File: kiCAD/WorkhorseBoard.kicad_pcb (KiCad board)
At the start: 2 copper layers, 392 parts, among them J1 USB_B_Mini, J10 MAIN_POWER, J11 BED_POWER, J12 H0, J13 F0, J14 V_SELECT, J15 F1, J16 F4, J17 H1, J18 V_SELECT, J19 F2, J2 Micro_SD_Card, J20 F5, J21 H2, J22 F3, J23 HB, J24 Conn_01x02, J25 Conn_01x02, J26 Conn_01x02, J27 Conn_01x02, J28 Conn_01x03, J29 Conn_01x03, J3 Conn_01x06, J30 Conn_01x03, J31 Conn_01x03, J32 Conn_01x03, J33 Conn_01x03, J4 X, J5 E0, J6 Y, J7 E1, J8 Z, J9 E2, Q1 Q_NMOS_GSD, Q10 Q_NMOS_GDS, Q2 Q_NMOS_GDS, Q3 Q_NMOS_GSD, Q4 Q_NMOS_GSD, Q5 Q_NMOS_GDS, Q6 Q_NMOS_GSD, Q7 Q_NMOS_GSD, Q8 Q_NMOS_GDS, Q9 Q_NMOS_GSD, SW1 SW_Push, U1 24C02, U10 TPS54531, U11 TPS54531, U12 AP7361C-33E-13, U13 74HCT365, U14 74HCT365, U2 USBLC6-2SC6, U3 STM32F446VETx, U4 TMC2209, U5 TMC2209, U6 TMC2209, U7 TMC2209, U8 TMC2209, U9 TMC2209, Y1 X322512MSB4SI

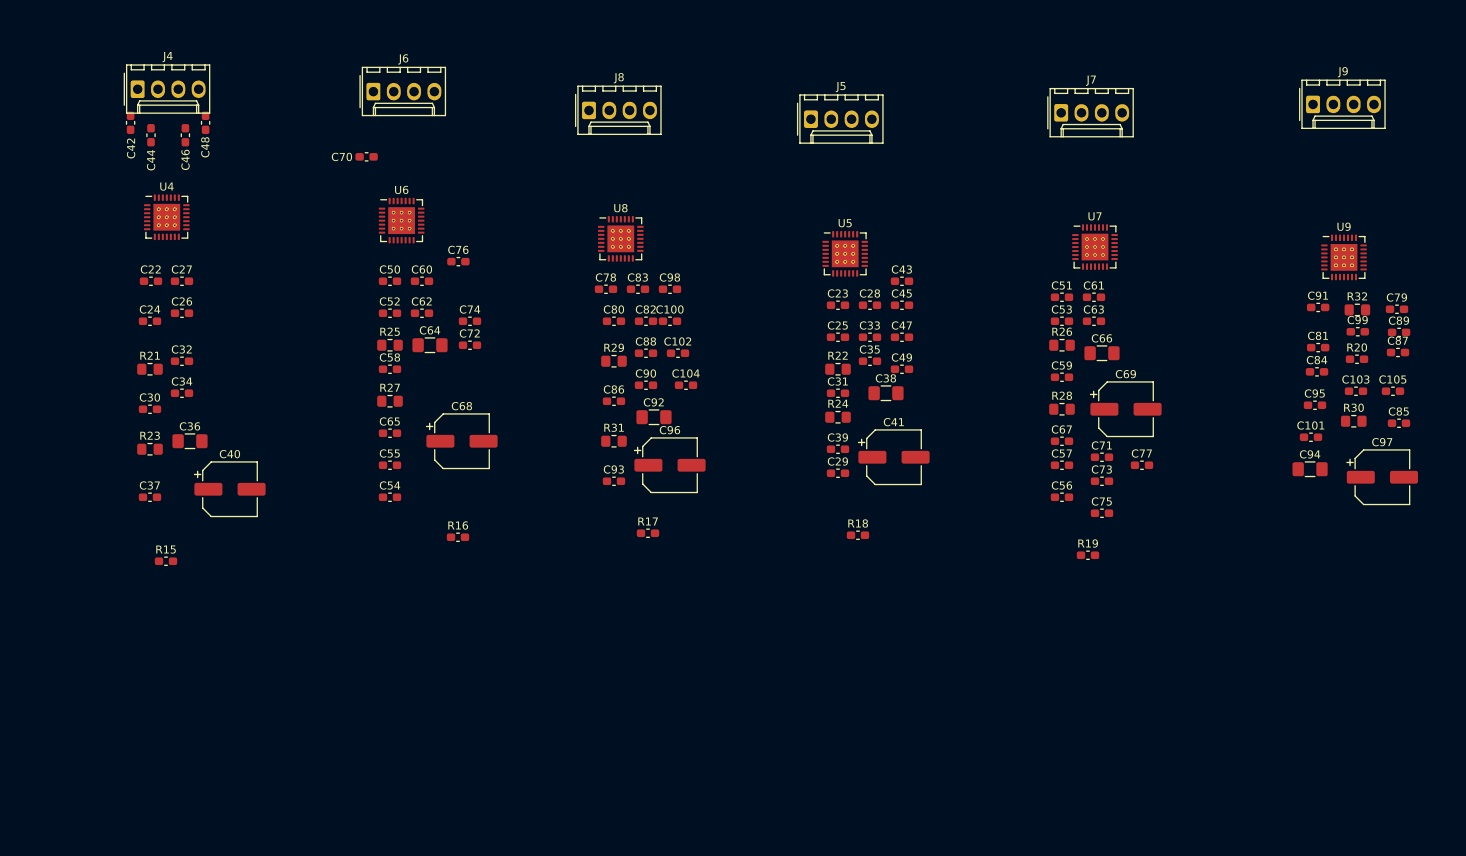
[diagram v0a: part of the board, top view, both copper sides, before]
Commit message: started laying out drivers
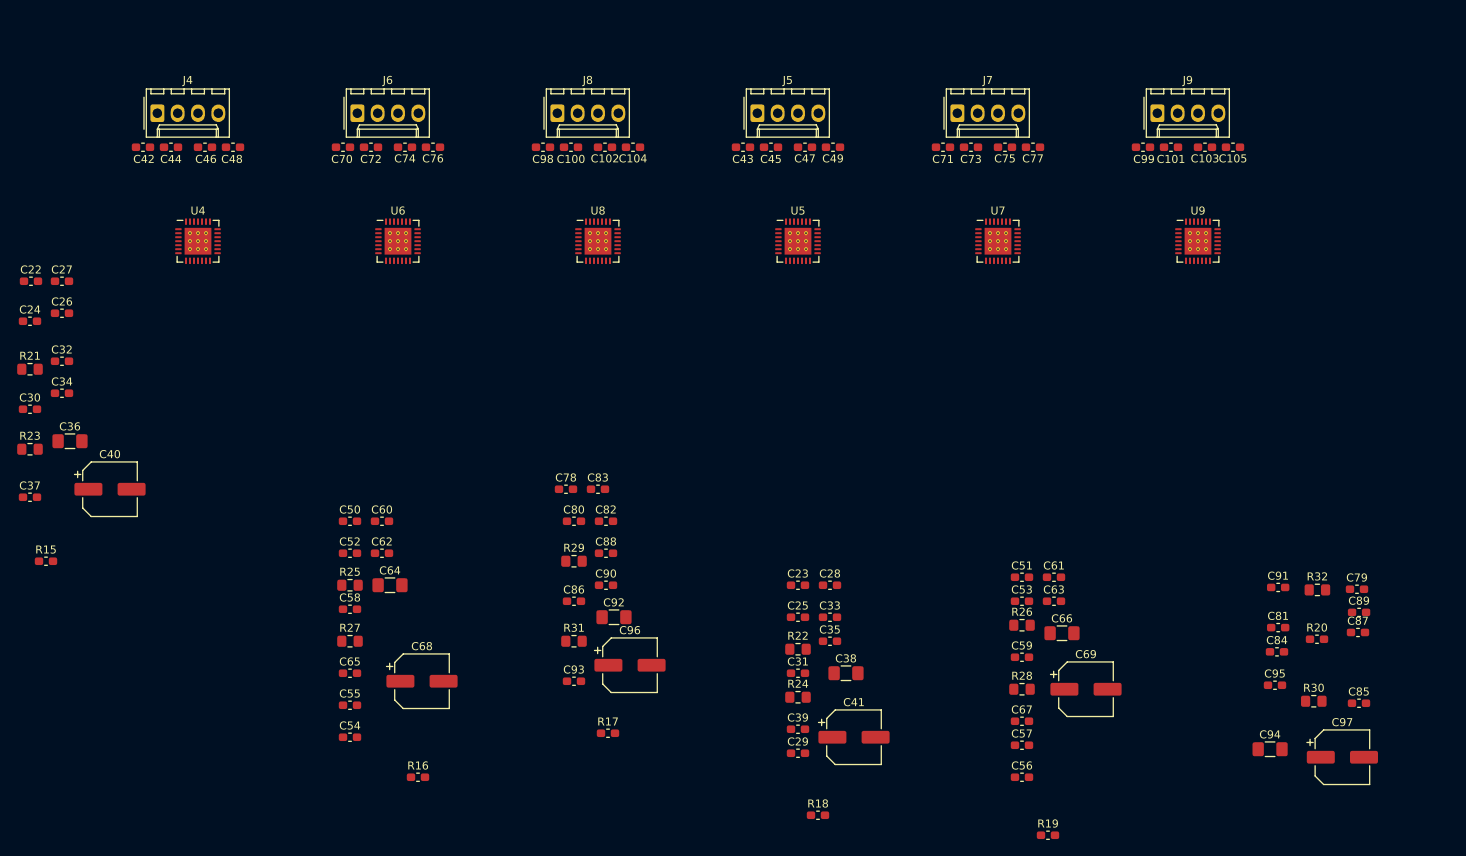
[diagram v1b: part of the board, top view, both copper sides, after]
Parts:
- moved C75 47.3 mm to (140.9, 38.2), turned to 180 degrees
- moved C73 44.8 mm to (136.6, 38.2)
- moved C71 43.5 mm to (133.1, 38.2)
- moved C77 42.0 mm to (144.4, 38.2), turned to 180 degrees
- moved C101 40.3 mm to (161.6, 38.2)
- moved C105 36.5 mm to (169.4, 38.2), turned to 180 degrees
- moved C103 35.9 mm to (165.9, 38.2), turned to 180 degrees
- moved C99 35.4 mm to (158.1, 38.2)
- moved C91 35.4 mm to (175.0, 93.3)
- moved C23 35.4 mm to (115.0, 93.0)
- moved C25 35.4 mm to (115.0, 97.0)
- moved C28 35.4 mm to (119.0, 93.0)
- moved C29 35.4 mm to (115.0, 114.0)
- moved C31 35.4 mm to (115.0, 104.0)
- moved C33 35.4 mm to (119.0, 97.0)
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
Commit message: layed out TMC's and started laying out power electronics
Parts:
- moved Q10 292.9 mm to (50.5, 177.2), turned to 180 degrees
- moved J23 277.1 mm to (36.5, 167.2), turned to 270 degrees
- moved H3 261.3 mm to (36.0, 189.2)
- moved C139 255.1 mm to (245.0, 134.8)
- moved D14 255.1 mm to (223.6, 125.4)
- moved D16 255.1 mm to (246.4, 146.3)
- moved D24 255.1 mm to (259.4, 132.5)
- moved D25 255.1 mm to (243.1, 138.5)
- moved J16 255.1 mm to (220.4, 149.3)
- moved J17 255.1 mm to (187.2, 146.3)
- moved JP6 255.1 mm to (242.7, 108.9)
- moved Q3 255.1 mm to (254.1, 121.2)
- moved Q6 255.1 mm to (262.6, 113.4)
- moved Q9 255.1 mm to (255.4, 116.7)
- moved R44 255.1 mm to (247.4, 137.7)
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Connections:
- C100 pad 2: Net-(C100-Pad2) -> Z_OB1
- C101 pad 2: Net-(C101-Pad2) -> E2_OB1
- C102 pad 2: Net-(C102-Pad2) -> Z_OA1
- C103 pad 2: Net-(C103-Pad2) -> E2_OA1
- C104 pad 2: Net-(C104-Pad2) -> Z_OA2
- C105 pad 2: Net-(C105-Pad2) -> E2_OA2
- C42 pad 2: Net-(C42-Pad2) -> X_OB2
- C43 pad 2: Net-(C43-Pad2) -> E0_OB2
- C44 pad 2: Net-(C44-Pad2) -> X_OB1
- C45 pad 2: Net-(C45-Pad2) -> E0_OB1
- C46 pad 2: Net-(C46-Pad2) -> X_OA1
- C47 pad 2: Net-(C47-Pad2) -> E0_OA1
- C48 pad 2: Net-(C48-Pad2) -> X_OA2
- C49 pad 2: Net-(C49-Pad2) -> E0_OA2
- C70 pad 2: Net-(C70-Pad2) -> Y_OB2
- C71 pad 2: Net-(C71-Pad2) -> E1_OB2
- C72 pad 2: Net-(C72-Pad2) -> Y_OB1
- C73 pad 2: Net-(C73-Pad2) -> E1_OB1
- C74 pad 2: Net-(C74-Pad2) -> Y_OA1
- C75 pad 2: Net-(C75-Pad2) -> E1_OA1
- C76 pad 2: Net-(C76-Pad2) -> Y_OA2
- C77 pad 2: Net-(C77-Pad2) -> E1_OA2
- C98 pad 2: Net-(C98-Pad2) -> Z_OB2
- C99 pad 2: Net-(C99-Pad2) -> E2_OB2
- J4 pad 1: Net-(C42-Pad2) -> X_OB2
- J4 pad 2: Net-(C44-Pad2) -> X_OB1
- J4 pad 3: Net-(C46-Pad2) -> X_OA1
- J4 pad 4: Net-(C48-Pad2) -> X_OA2
- J5 pad 1: Net-(C43-Pad2) -> E0_OB2
- J5 pad 2: Net-(C45-Pad2) -> E0_OB1
- J5 pad 3: Net-(C47-Pad2) -> E0_OA1
- J5 pad 4: Net-(C49-Pad2) -> E0_OA2
- J6 pad 1: Net-(C70-Pad2) -> Y_OB2
- J6 pad 2: Net-(C72-Pad2) -> Y_OB1
- J6 pad 3: Net-(C74-Pad2) -> Y_OA1
- J6 pad 4: Net-(C76-Pad2) -> Y_OA2
- J7 pad 1: Net-(C71-Pad2) -> E1_OB2
- J7 pad 2: Net-(C73-Pad2) -> E1_OB1
- J7 pad 3: Net-(C75-Pad2) -> E1_OA1
- J7 pad 4: Net-(C77-Pad2) -> E1_OA2
- J8 pad 1: Net-(C98-Pad2) -> Z_OB2
- J8 pad 2: Net-(C100-Pad2) -> Z_OB1
- J8 pad 3: Net-(C102-Pad2) -> Z_OA1
- J8 pad 4: Net-(C104-Pad2) -> Z_OA2
- J9 pad 1: Net-(C99-Pad2) -> E2_OB2
- J9 pad 2: Net-(C101-Pad2) -> E2_OB1
- J9 pad 3: Net-(C103-Pad2) -> E2_OA1
- J9 pad 4: Net-(C105-Pad2) -> E2_OA2
- U4 pad 1: Net-(C48-Pad2) -> X_OB2
- U4 pad 21: Net-(C44-Pad2) -> X_OA2
- U4 pad 24: Net-(C42-Pad2) -> X_OA1
- U4 pad 26: Net-(C46-Pad2) -> X_OB1
- U5 pad 1: Net-(C49-Pad2) -> E0_OB2
- U5 pad 21: Net-(C45-Pad2) -> E0_OA2
- U5 pad 24: Net-(C43-Pad2) -> E0_OA1
- U5 pad 26: Net-(C47-Pad2) -> E0_OB1
- U6 pad 1: Net-(C76-Pad2) -> Y_OB2
- U6 pad 21: Net-(C72-Pad2) -> Y_OA2
- U6 pad 24: Net-(C70-Pad2) -> Y_OA1
- U6 pad 26: Net-(C74-Pad2) -> Y_OB1
- U7 pad 1: Net-(C77-Pad2) -> E1_OB2
- U7 pad 21: Net-(C73-Pad2) -> E1_OA2
- U7 pad 24: Net-(C71-Pad2) -> E1_OA1
- U7 pad 26: Net-(C75-Pad2) -> E1_OB1
- U8 pad 1: Net-(C104-Pad2) -> Z_OB2
- U8 pad 21: Net-(C100-Pad2) -> Z_OA2
- U8 pad 24: Net-(C98-Pad2) -> Z_OA1
- U8 pad 26: Net-(C102-Pad2) -> Z_OB1
- U9 pad 1: Net-(C105-Pad2) -> E2_OB2
- U9 pad 21: Net-(C101-Pad2) -> E2_OA2
- U9 pad 24: Net-(C99-Pad2) -> E2_OA1
- U9 pad 26: Net-(C103-Pad2) -> E2_OB1

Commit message: fixed placement slightly to improve cooling
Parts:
- moved C107 323.1 mm to (318.9, -26.2)
- moved C109 323.1 mm to (318.9, -24.6)
- moved C111 323.1 mm to (318.2, -29.5)
- moved D2 323.1 mm to (315.2, -29.1)
- moved F3 323.1 mm to (307.9, -24.9)
- moved J11 323.1 mm to (297.5, -46.4)
- moved J23 323.1 mm to (297.5, -23.1)
- moved Q10 323.1 mm to (311.5, -13.2)
- moved D4 313.3 mm to (320.2, -32.7), turned to 270 degrees
- moved R34 308.0 mm to (320.3, -28.9), turned to 90 degrees
- moved D9 63.8 mm to (66.0, 104.4), turned to 180 degrees
- moved D8 56.6 mm to (66.0, 122.9), turned to 180 degrees
- moved C124 34.0 mm to (67.5, 127.2), turned to 180 degrees
- moved C89 27.5 mm to (198.6, 41.2), turned to 180 degrees
- moved C79 27.1 mm to (218.6, 55.5)
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
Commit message: did layout for FETs and redid layout for Power input
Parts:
- removed J14, J18: V_SELECT, Connector_PinHeader_2.54mm:PinHeader_2x03_P2.54mm_Vertical
- added JP19: Jumper_3_Open, Connector_PinHeader_2.54mm:PinHeader_1x03_P2.54mm_Vertical, F.Cu at (153.8, 104.0)
- added JP20: Jumper_3_Open, Connector_PinHeader_2.54mm:PinHeader_1x03_P2.54mm_Vertical, F.Cu at (163.0, 104.0)
- moved D4 294.2 mm to (48.2, 79.5)
- moved R34 294.1 mm to (48.2, 82.9)
- moved Q10 291.9 mm to (49.6, 115.8)
- moved D2 291.1 mm to (45.8, 81.0)
- moved F3 289.8 mm to (45.9, 98.8)
- moved J11 288.7 mm to (35.5, 74.8)
- moved J23 288.7 mm to (35.5, 98.1)
- moved C107 288.6 mm to (51.9, 83.3)
- moved C109 288.6 mm to (51.9, 84.9)
- moved C111 288.3 mm to (51.5, 80.0)
- moved D36 208.3 mm to (48.6, 120.2)
- moved C147 204.4 mm to (48.5, 105.0), turned to 90 degrees
- moved R67 201.8 mm to (50.8, 104.6), turned to 270 degrees
- moved R47 197.7 mm to (250.4, 71.8)
- moved R53 197.7 mm to (246.1, 71.8)
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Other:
- copper layers 2 -> 4

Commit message: finished layout of everything but endstops.
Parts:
- removed C18: 100n, Capacitor_SMD:C_0603_1608Metric_Pad1.05x0.95mm_HandSolder
- removed C19: 1u, Capacitor_SMD:C_0603_1608Metric_Pad1.05x0.95mm_HandSolder
- removed D13, D18, D25: LED_Small, Diode_SMD:D_0603_1608Metric_Pad1.05x0.95mm_HandSolder
- removed R56, R60, R64: 2.2k, Resistor_SMD:R_0603_1608Metric_Pad1.05x0.95mm_HandSolder
- moved JP13 195.0 mm to (334.7, 92.2), turned to 90 degrees
- moved JP17 183.3 mm to (318.2, 92.8), turned to 90 degrees
- moved R18 180.3 mm to (126.2, 93.1), turned to 90 degrees
- moved SWD1 179.7 mm to (208.8, 113.8), turned to 90 degrees
- moved UART1 178.7 mm to (217.3, 122.5), turned to 270 degrees
- moved JP10 178.5 mm to (335.0, 75.2), turned to 90 degrees
- moved JP18 177.4 mm to (318.5, 75.8), turned to 90 degrees
- moved C152 177.1 mm to (374.9, 74.2)
- moved C153 177.1 mm to (370.6, 78.8)
- moved C154 177.1 mm to (365.9, 83.5)
- moved C155 177.1 mm to (379.9, 70.9)
- moved C156 177.1 mm to (370.3, 81.3)
- moved C157 177.1 mm to (374.9, 76.7)
- moved D41 177.1 mm to (375.6, 66.6)
- moved D42 177.1 mm to (361.6, 81.0)
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
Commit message: Started tracing
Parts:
- moved C155 196.9 mm to (183.8, 89.1), turned to 90 degrees
- moved JP12 195.8 mm to (186.5, 87.5)
- moved R88 192.9 mm to (187.5, 81.9), turned to 270 degrees
- moved R80 192.8 mm to (187.4, 70.1), turned to 270 degrees
- moved C152 191.5 mm to (183.7, 65.6), turned to 90 degrees
- moved R87 188.6 mm to (191.8, 93.6), turned to 90 degrees
- moved C156 186.6 mm to (183.8, 77.4), turned to 90 degrees
- moved D41 185.4 mm to (190.2, 70.1), turned to 270 degrees
- moved JP7 180.0 mm to (186.4, 64.0)
- moved R85 178.9 mm to (187.5, 93.6), turned to 270 degrees
- moved R90 178.3 mm to (192.0, 81.9), turned to 90 degrees
- moved C157 172.2 mm to (203.2, 89.4), turned to 90 degrees
- moved JP15 170.6 mm to (186.5, 75.7)
- moved R82 170.2 mm to (191.7, 70.1), turned to 90 degrees
- moved R89 170.0 mm to (207.0, 93.9), turned to 270 degrees
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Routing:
- net GND: track 0.00 -> 358.9 mm, vias 0 -> 3
- net +24V: track 0.00 -> 173.6 mm
- net +3V3: track 0.00 -> 138.5 mm
- net +5V: track 0.00 -> 134.1 mm
- net VM: track 0.00 -> 96.4 mm
- net Net-(Q10-Pad1): track 0.00 -> 90.5 mm, vias 0 -> 2
- net +12V: track 0.00 -> 87.0 mm
- net VBED: track 0.00 -> 46.1 mm
- net Net-(Q2-Pad1): track 0.00 -> 31.2 mm, vias 0 -> 2
- net Net-(C147-Pad1): track 0.00 -> 30.6 mm
- net Net-(C138-Pad1): track 0.00 -> 27.0 mm
- net Net-(C144-Pad1): track 0.00 -> 25.5 mm
- net Net-(C142-Pad1): track 0.00 -> 24.7 mm
- net Net-(C129-Pad1): track 0.00 -> 21.7 mm
- net Net-(C128-Pad1): track 0.00 -> 20.5 mm
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- added copper zone on F.Cu, net +12V
- added copper zone on F.Cu, net +24V
- added copper zone on F.Cu, net +3V3
- added copper zone on F.Cu, net +5V
- added copper zone on B.Cu, net GND
- added copper zone on F.Cu, net GND
- added copper zone on In1.Cu, net GND
- added copper zone on F.Cu, net VM
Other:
- board outline added: 205 x 97 mm

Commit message: small changes.
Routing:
- net +24V: track 173.6 -> 248.9 mm
- net VM: track 96.4 -> 98.4 mm
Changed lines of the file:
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@@
     (thickness 1.6)
     (drawings 9)
-    (tracks 1137)
+    (tracks 1172)
     (zones 0)
     (modules 384)
@@
   (segment (start 166.5 41.25) (end 166.5 38.25) (width 0.5) (layer F.Cu) (net 15))
   (segment (start 196.5 41.25) (end 196.5 38.25) (width 0.5) (layer F.Cu) (net 15))
+  (segment (start 184.75 48) (end 184.75 46) (width 0.5) (layer F.Cu) (net 15))
   (segment (start 54.05 54) (end 49.812986 54) (width 0.3) (layer F.Cu) (net 16))
   (segment (start 48.312986 52.5) (end 48 52.5) (width 0.3) (layer F.Cu) (net 16))
@@
   (segment (start 59.5 68.5) (end 61.25 70.25) (width 0.7) (layer F.Cu) (net 49))
   (segment (start 59.5 66.75) (end 59.5 68.5) (width 0.7) (layer F.Cu) (net 49))
-  (segment (start 78.5 108.5) (end 78.5 106.25) (width 1) (layer F.Cu) (net 49))
   (segment (start 81.5 109.5) (end 79.5 109.5) (width 1) (layer F.Cu) (net 49))
   (segment (start 79.5 109.5) (end 78.5 108.5) (width 1) (layer F.Cu) (net 49))
@@
   (segment (start 41.5 76.25) (end 50.25 76.25) (width 0.5) (layer F.Cu) (net 49))
   (segment (start 50.25 76.25) (end 53.75 79.75) (width 0.5) (layer F.Cu) (net 49))
+  (segment (start 79.5 113.14) (end 80.5 114.14) (width 2) (layer F.Cu) (net 49))
+  (segment (start 79.5 109.5) (end 79.5 109.75) (width 2) (layer F.Cu) (net 49))
+  (segment (start 79.5 109.75) (end 80.25 110.5) (width 2) (layer F.Cu) (net 49))
+  (segment (start 80.25 111) (end 79.5 111.75) (width 2) (layer F.Cu) (net 49))
+  (segment (start 80.25 110.5) (end 80.25 111) (width 2) (layer F.Cu) (net 49))
+  (segment (start 79.5 111.75) (end 79.5 113.14) (width 2) (layer F.Cu) (net 49))
+  (segment (start 80.75 109.5) (end 78.5 107.25) (width 2) (layer F.Cu) (net 49))
+  (segment (start 78.5 108.5) (end 78.5 107.25) (width 1) (layer F.Cu) (net 49))
+  (segment (start 81.5 109.5) (end 80.75 109.5) (width 2) (layer F.Cu) (net 49))
+  (segment (start 78.5 107.25) (end 78.5 106.25) (width 1) (layer F.Cu) (net 49))
+  (segment (start 99.5 109.25) (end 96.5 106.25) (width 2) (layer F.Cu) (net 49))
+  (segment (start 63.5 109.25) (end 60.5 106.25) (width 2) (layer F.Cu) (net 49))
+  (segment (start 63.5 109.5) (end 63.5 109.25) (width 2) (layer F.Cu) (net 49))
+  (segment (start 81.5 109.25) (end 78.5 106.25) (width 2) (layer F.Cu) (net 49))
+  (segment (start 81.5 109.5) (end 81.5 109.25) (width 2) (layer F.Cu) (net 49))
+  (segment (start 98.5 113.89) (end 95.64 113.89) (width 2) (layer F.Cu) (net 49))
+  (segment (start 95.64 113.89) (end 94.75 113) (width 2) (layer F.Cu) (net 49))
+  (segment (start 94.75 113) (end 94.75 106.25) (width 2) (layer F.Cu) (net 49))
+  (segment (start 94.75 106.25) (end 96.5 106.25) (width 2) (layer F.Cu) (net 49))
+  (segment (start 76.5 106.25) (end 78.5 106.25) (width 2) (layer F.Cu) (net 49))
+  (segment (start 76.5 108.25) (end 77.25 108.25) (width 2) (layer F.Cu) (net 49))
+  (segment (start 76.5 108.25) (end 76.5 106.25) (width 2) (layer F.Cu) (net 49))
+  (segment (start 77.25 108.25) (end 78.75 109.75) (width 2) (layer F.Cu) (net 49))
+  (segment (start 78.75 109.75) (end 78.75 110.75) (width 2) (layer F.Cu) (net 49))
+  (segment (start 78.75 110.75) (end 78.25 111.25) (width 2) (layer F.Cu) (net 49))
+  (segment (start 77.64 114.14) (end 76.5 113) (width 2) (layer F.Cu) (net 49))
+  (segment (start 80.5 114.14) (end 77.64 114.14) (width 2) (layer F.Cu) (net 49))
+  (segment (start 76.5 113) (end 76.5 108.25) (width 2) (layer F.Cu) (net 49))
+  (segment (start 80.5 114.14) (end 79.89 114.14) (width 2) (layer F.Cu) (net 49))
+  (segment (start 78.5 112.75) (end 78.5 106.25) (width 2) (layer F.Cu) (net 49))
+  (segment (start 79.89 114.14) (end 78.5 112.75) (width 2) (layer F.Cu) (net 49))
+  (segment (start 62.5 114.14) (end 60.14 114.14) (width 2) (layer F.Cu) (net 49))
+  (segment (start 60.14 114.14) (end 58.5 112.5) (width 2) (layer F.Cu) (net 49))
+  (segment (start 58.5 112.5) (end 58.5 106.25) (width 2) (layer F.Cu) (net 49))
+  (segment (start 58.5 106.25) (end 60.5 106.25) (width 2) (layer F.Cu) (net 49))
   (segment (start 35.5 98.1) (end 40.1 98.1) (width 3) (layer F.Cu) (net 50))
   (segment (start 42.25 100.25) (end 45.5 100.25) (width 3) (layer F.Cu) (net 50))
@@
       )
     )
+  )
+  (zone (net 49) (net_name +24V) (layer F.Cu) (hatch edge 0.508)
+    (connect_pads (clearance 0.508))
+    (min_thickness 0.254)
+    (fill yes (arc_segments 32) (thermal_gap 0.508) (thermal_bridge_width 0.508))
+    (polygon
+      (pts
+        (xy 80 109.25) (xy 79.25 114.25) (xy 77.5 114.25) (xy 76.25 112.75) (xy 76.5 106.5)
+        (xy 79.25 106.5)
+      )
+    )
